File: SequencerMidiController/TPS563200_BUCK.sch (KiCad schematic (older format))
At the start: 13 parts, among them U38 TPS563200

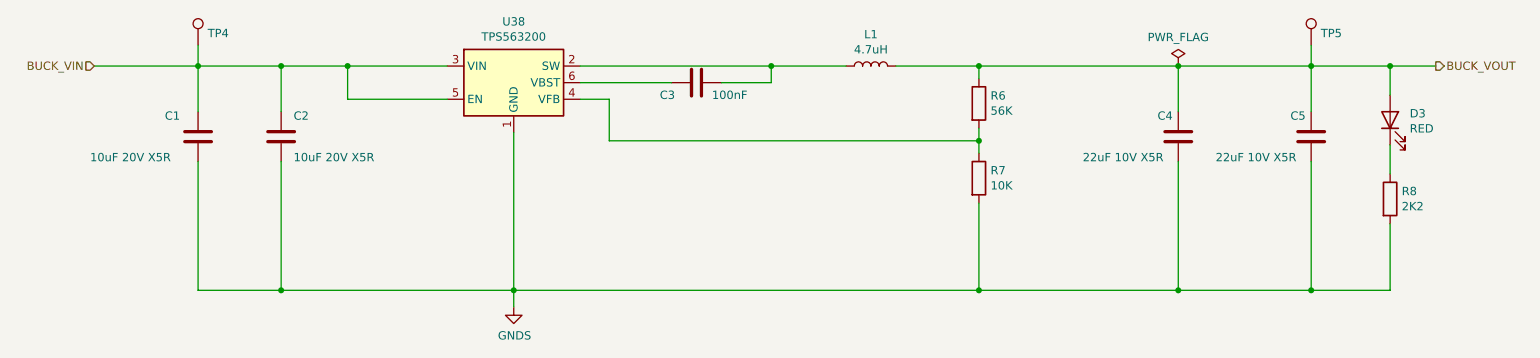
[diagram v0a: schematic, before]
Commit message: RevA Layout draft completed
- Needs tidy up
- Add test points
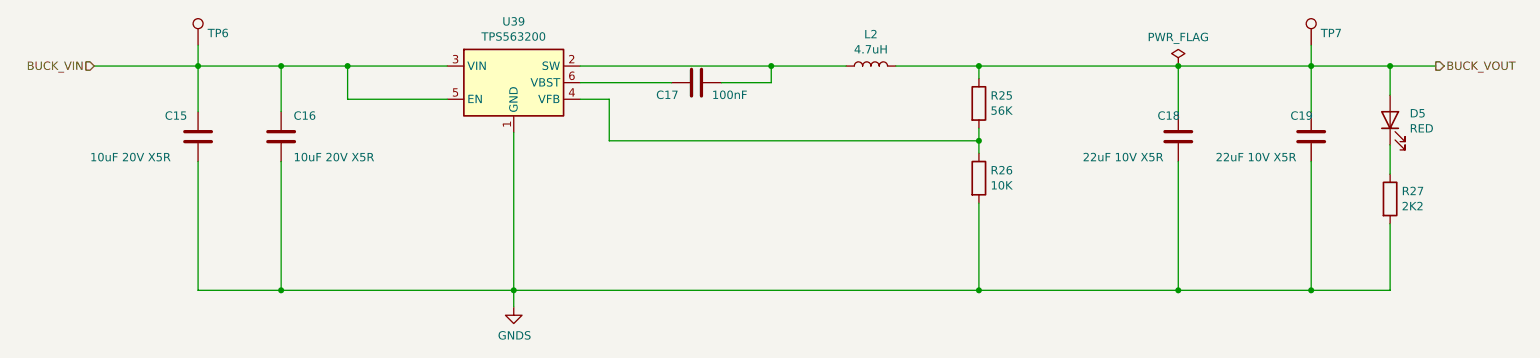
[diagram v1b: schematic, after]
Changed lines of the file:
@@
 AR Path="/60BD3123/60BD5AA5/60BD5C0D" Ref="U38"  Part="1"
 AR Path="/60BD3123/63615DFB/60BD5C0D" Ref="U39"  Part="1"
-F 0 "U38" H 4150 3667 50  0000 C CNN
+F 0 "U39" H 4150 3667 50  0000 C CNN
 F 1 "TPS563200" H 4150 3576 50  0000 C CNN
 F 2 "Package_TO_SOT_SMD:SOT-23-6" H 4200 3050 50  0001 L CNN
 F 3 "http://www.ti.com/lit/ds/symlink/tps563200.pdf" H 4175 3750 50  0001 C CNN
+F 4 "~" H 4150 3300 50  0001 C CNN "LcscNo"
+F 5 "~" H 4150 3300 50  0001 C CNN "Type"
 	1    4150 3300
 	1    0    0    -1
@@
 AR Path="/60BD3123/60BD5AA5/60BD6656" Ref="#PWR0108"  Part="1"
 AR Path="/60BD3123/63615DFB/60BD6656" Ref="#PWR023"  Part="1"
-F 0 "#PWR0108" H 4150 4400 50  0001 C CNN
+F 0 "#PWR023" H 4150 4400 50  0001 C CNN
 F 1 "GNDS" H 4155 4477 50  0000 C CNN
 F 2 "" H 4150 4650 50  0001 C CNN
@@
 AR Path="/60BD3123/60BD5AA5/60BD6867" Ref="C1"  Part="1"
 AR Path="/60BD3123/63615DFB/60BD6867" Ref="C15"  Part="1"
-F 0 "C1" H 2050 3750 50  0000 L CNN
+F 0 "C15" H 2050 3750 50  0000 L CNN
 F 1 "10uF 20V X5R" H 1600 3500 50  0000 L CNN
 F 2 "Resistor_SMD:R_1206_3216Metric_Pad1.30x1.75mm_HandSolder" H 2288 3475 50  0001 C CNN
 F 3 "~" H 2250 3625 50  0001 C CNN
+F 4 "~" H 2250 3625 50  0001 C CNN "LcscNo"
+F 5 "~" H 2250 3625 50  0001 C CNN "Type"
 	1    2250 3625
 	1    0    0    -1
@@
 AR Path="/60BD3123/60BD5AA5/60BD7269" Ref="C2"  Part="1"
 AR Path="/60BD3123/63615DFB/60BD7269" Ref="C16"  Part="1"
-F 0 "C2" H 2825 3750 50  0000 L CNN
+F 0 "C16" H 2825 3750 50  0000 L CNN
 F 1 "10uF 20V X5R" H 2825 3500 50  0000 L CNN
 F 2 "Resistor_SMD:R_1206_3216Metric_Pad1.30x1.75mm_HandSolder" H 2788 3475 50  0001 C CNN
 F 3 "~" H 2750 3625 50  0001 C CNN
+F 4 "~" H 2750 3625 50  0001 C CNN "LcscNo"
+F 5 "~" H 2750 3625 50  0001 C CNN "Type"
 	1    2750 3625
 	1    0    0    -1
@@
 AR Path="/60BD3123/60BD5AA5/60BD7D8E" Ref="L1"  Part="1"
 AR Path="/60BD3123/63615DFB/60BD7D8E" Ref="L2"  Part="1"
-F 0 "L1" V 6490 3200 50  0000 C CNN
+F 0 "L2" V 6490 3200 50  0000 C CNN
 F 1 "4.7uH" V 6399 3200 50  0000 C CNN
 F 2 "Inductor_SMD:L_Taiyo-Yuden_NR-80xx_HandSoldering" H 6300 3200 50  0001 C CNN
 F 3 "https://datasheet.lcsc.com/lcsc/1808311234_SXN-Shun-Xiang-Nuo-Elec-SMNR6028-4R7MT_C266428.pdf" H 6300 3200 50  0001 C CNN
 F 4 "C266428" H 6300 3200 50  0001 C CNN "LcscNo"
+F 5 "~" H 6300 3200 50  0001 C CNN "Type"
 	1    6300 3200
 	0    -1   -1   0
@@
 AR Path="/60BD3123/60BD5AA5/60C2B2AA" Ref="C3"  Part="1"
 AR Path="/60BD3123/63615DFB/60C2B2AA" Ref="C17"  Part="1"
-F 0 "C3" V 5175 3475 50  0000 C CNN
+F 0 "C17" V 5175 3475 50  0000 C CNN
 F 1 "100nF" V 5175 3100 50  0000 C CNN
 F 2 "Capacitor_SMD:C_0805_2012Metric_Pad1.18x1.45mm_HandSolder" H 5288 3150 50  0001 C CNN
 F 3 "~" H 5250 3300 50  0001 C CNN
+F 4 "~" H 5250 3300 50  0001 C CNN "LcscNo"
+F 5 "~" H 5250 3300 50  0001 C CNN "Type"
 	1    5250 3300
 	0    -1   -1   0
@@
 AR Path="/60BD3123/60BD5AA5/60C2D3AE" Ref="R6"  Part="1"
 AR Path="/60BD3123/63615DFB/60C2D3AE" Ref="R25"  Part="1"
-F 0 "R6" H 7020 3471 50  0000 L CNN
+F 0 "R25" H 7020 3471 50  0000 L CNN
 F 1 "56K" H 7020 3380 50  0000 L CNN
 F 2 "Resistor_SMD:R_0805_2012Metric_Pad1.20x1.40mm_HandSolder" V 6880 3425 50  0001 C CNN
 F 3 "~" H 6950 3425 50  0001 C CNN
+F 4 "~" H 6950 3425 50  0001 C CNN "LcscNo"
+F 5 "~" H 6950 3425 50  0001 C CNN "Type"
 	1    6950 3425
 	1    0    0    -1
@@
 AR Path="/60BD3123/60BD5AA5/60C2DA69" Ref="R7"  Part="1"
 AR Path="/60BD3123/63615DFB/60C2DA69" Ref="R26"  Part="1"
-F 0 "R7" H 7020 3921 50  0000 L CNN
+F 0 "R26" H 7020 3921 50  0000 L CNN
 F 1 "10K" H 7020 3830 50  0000 L CNN
 F 2 "Resistor_SMD:R_0805_2012Metric_Pad1.20x1.40mm_HandSolder" V 6880 3875 50  0001 C CNN
 F 3 "~" H 6950 3875 50  0001 C CNN
+F 4 "~" H 6950 3875 50  0001 C CNN "LcscNo"
+F 5 "~" H 6950 3875 50  0001 C CNN "Type"
 	1    6950 3875
 	1    0    0    -1
@@
 AR Path="/60BD3123/60BD5AA5/60C31AEB" Ref="C4"  Part="1"
 AR Path="/60BD3123/63615DFB/60C31AEB" Ref="C18"  Part="1"
-F 0 "C4" H 8025 3750 50  0000 L CNN
+F 0 "C18" H 8025 3750 50  0000 L CNN
 F 1 "22uF 10V X5R" H 7575 3500 50  0000 L CNN
 F 2 "Resistor_SMD:R_1206_3216Metric_Pad1.30x1.75mm_HandSolder" H 8188 3475 50  0001 C CNN
 F 3 "~" H 8150 3625 50  0001 C CNN
+F 4 "~" H 8150 3625 50  0001 C CNN "LcscNo"
+F 5 "~" H 8150 3625 50  0001 C CNN "Type"
 	1    8150 3625
 	1    0    0    -1
@@
 AR Path="/60BD3123/60BD5AA5/60C31AF1" Ref="C5"  Part="1"
 AR Path="/60BD3123/63615DFB/60C31AF1" Ref="C19"  Part="1"
-F 0 "C5" H 8825 3750 50  0000 L CNN
+F 0 "C19" H 8825 3750 50  0000 L CNN
 F 1 "22uF 10V X5R" H 8375 3500 50  0000 L CNN
 F 2 "Resistor_SMD:R_1206_3216Metric_Pad1.30x1.75mm_HandSolder" H 8988 3475 50  0001 C CNN
 F 3 "~" H 8950 3625 50  0001 C CNN
+F 4 "~" H 8950 3625 50  0001 C CNN "LcscNo"
+F 5 "~" H 8950 3625 50  0001 C CNN "Type"
 	1    8950 3625
 	1    0    0    -1
@@
 AR Path="/60BD3123/60BD5AA5/60C3B029" Ref="TP5"  Part="1"
 AR Path="/60BD3123/63615DFB/60C3B029" Ref="TP7"  Part="1"
-F 0 "TP5" H 9008 3147 50  0000 L CNN
+F 0 "TP7" H 9008 3147 50  0000 L CNN
 F 1 "TestPoint" H 9008 3102 50  0001 L CNN
 F 2 "TestPoint:TestPoint_Pad_D1.0mm" H 9150 3075 50  0001 C CNN
 F 3 "~" H 9150 3075 50  0001 C CNN
+F 4 "~" H 8950 3075 50  0001 C CNN "LcscNo"
+F 5 "~" H 8950 3075 50  0001 C CNN "Type"
 	1    8950 3075
 	1    0    0    -1
@@
 AR Path="/60BD3123/60BD5AA5/60C3C725" Ref="TP4"  Part="1"
 AR Path="/60BD3123/63615DFB/60C3C725" Ref="TP6"  Part="1"
-F 0 "TP4" H 2308 3147 50  0000 L CNN
+F 0 "TP6" H 2308 3147 50  0000 L CNN
 F 1 "TestPoint" H 2308 3102 50  0001 L CNN
 F 2 "TestPoint:TestPoint_Pad_D1.0mm" H 2450 3075 50  0001 C CNN
 F 3 "~" H 2450 3075 50  0001 C CNN
+F 4 "~" H 2250 3075 50  0001 C CNN "LcscNo"
+F 5 "~" H 2250 3075 50  0001 C CNN "Type"
 	1    2250 3075
 	1    0    0    -1
@@
 AR Path="/60BD3123/60BD5AA5/60C4D84C" Ref="D3"  Part="1"
 AR Path="/60BD3123/63615DFB/60C4D84C" Ref="D5"  Part="1"
-F 0 "D3" V 9464 3407 50  0000 R CNN
+F 0 "D5" V 9464 3407 50  0000 R CNN
 F 1 "RED" V 9373 3407 50  0000 R CNN
 F 2 "LED_SMD:LED_0805_2012Metric_Pad1.15x1.40mm_HandSolder" H 9425 3525 50  0001 C CNN
 F 3 "~" H 9425 3525 50  0001 C CNN
 F 4 "C2293" H 9425 3525 50  0001 C CNN "LcscNo"
+F 5 "~" H 9425 3525 50  0001 C CNN "Type"
 	1    9425 3525
 	0    -1   -1   0
@@
 AR Path="/60BD3123/60BD5AA5/60C4D852" Ref="R8"  Part="1"
 AR Path="/60BD3123/63615DFB/60C4D852" Ref="R27"  Part="1"
-F 0 "R8" H 9495 4046 50  0000 L CNN
+F 0 "R27" H 9495 4046 50  0000 L CNN
 F 1 "2K2" H 9495 3955 50  0000 L CNN
 F 2 "Resistor_SMD:R_0805_2012Metric_Pad1.20x1.40mm_HandSolder" V 9355 4000 50  0001 C CNN
 F 3 "~" H 9425 4000 50  0001 C CNN
+F 4 "~" H 9425 4000 50  0001 C CNN "LcscNo"
+F 5 "~" H 9425 4000 50  0001 C CNN "Type"
 	1    9425 4000
 	1    0    0    -1
@@
 AR Path="/60BD3123/63615DFB/68A60987" Ref="#FLG0104"  Part="1"
 AR Path="/60BD3123/60BD5AA5/68A60987" Ref="#FLG0103"  Part="1"
-F 0 "#FLG0103" H 8150 3275 50  0001 C CNN
+F 0 "#FLG0104" H 8150 3275 50  0001 C CNN
 F 1 "PWR_FLAG" H 8150 3373 50  0000 C CNN
 F 2 "" H 8150 3200 50  0001 C CNN

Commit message: Completed RevA layout
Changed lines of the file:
@@
 AR Path="/60BD3123/60BD5AA5/60BD5C0D" Ref="U38"  Part="1"
 AR Path="/60BD3123/63615DFB/60BD5C0D" Ref="U39"  Part="1"
-F 0 "U39" H 4150 3667 50  0000 C CNN
+F 0 "U38" H 4150 3667 50  0000 C CNN
 F 1 "TPS563200" H 4150 3576 50  0000 C CNN
 F 2 "Package_TO_SOT_SMD:SOT-23-6" H 4200 3050 50  0001 L CNN
@@
 AR Path="/60BD3123/60BD5AA5/60BD6656" Ref="#PWR0108"  Part="1"
 AR Path="/60BD3123/63615DFB/60BD6656" Ref="#PWR023"  Part="1"
-F 0 "#PWR023" H 4150 4400 50  0001 C CNN
+F 0 "#PWR0108" H 4150 4400 50  0001 C CNN
 F 1 "GNDS" H 4155 4477 50  0000 C CNN
 F 2 "" H 4150 4650 50  0001 C CNN
@@
 AR Path="/60BD3123/60BD5AA5/60BD6867" Ref="C1"  Part="1"
 AR Path="/60BD3123/63615DFB/60BD6867" Ref="C15"  Part="1"
-F 0 "C15" H 2050 3750 50  0000 L CNN
+F 0 "C1" H 2050 3750 50  0000 L CNN
 F 1 "10uF 20V X5R" H 1600 3500 50  0000 L CNN
 F 2 "Resistor_SMD:R_1206_3216Metric_Pad1.30x1.75mm_HandSolder" H 2288 3475 50  0001 C CNN
@@
 AR Path="/60BD3123/60BD5AA5/60BD7269" Ref="C2"  Part="1"
 AR Path="/60BD3123/63615DFB/60BD7269" Ref="C16"  Part="1"
-F 0 "C16" H 2825 3750 50  0000 L CNN
+F 0 "C2" H 2825 3750 50  0000 L CNN
 F 1 "10uF 20V X5R" H 2825 3500 50  0000 L CNN
 F 2 "Resistor_SMD:R_1206_3216Metric_Pad1.30x1.75mm_HandSolder" H 2788 3475 50  0001 C CNN
@@
 AR Path="/60BD3123/60BD5AA5/60BD7D8E" Ref="L1"  Part="1"
 AR Path="/60BD3123/63615DFB/60BD7D8E" Ref="L2"  Part="1"
-F 0 "L2" V 6490 3200 50  0000 C CNN
+F 0 "L1" V 6490 3200 50  0000 C CNN
 F 1 "4.7uH" V 6399 3200 50  0000 C CNN
 F 2 "Inductor_SMD:L_Taiyo-Yuden_NR-80xx_HandSoldering" H 6300 3200 50  0001 C CNN
@@
 AR Path="/60BD3123/60BD5AA5/60C2B2AA" Ref="C3"  Part="1"
 AR Path="/60BD3123/63615DFB/60C2B2AA" Ref="C17"  Part="1"
-F 0 "C17" V 5175 3475 50  0000 C CNN
+F 0 "C3" V 5175 3475 50  0000 C CNN
 F 1 "100nF" V 5175 3100 50  0000 C CNN
 F 2 "Capacitor_SMD:C_0805_2012Metric_Pad1.18x1.45mm_HandSolder" H 5288 3150 50  0001 C CNN
@@
 AR Path="/60BD3123/60BD5AA5/60C2D3AE" Ref="R6"  Part="1"
 AR Path="/60BD3123/63615DFB/60C2D3AE" Ref="R25"  Part="1"
-F 0 "R25" H 7020 3471 50  0000 L CNN
+F 0 "R6" H 7020 3471 50  0000 L CNN
 F 1 "56K" H 7020 3380 50  0000 L CNN
 F 2 "Resistor_SMD:R_0805_2012Metric_Pad1.20x1.40mm_HandSolder" V 6880 3425 50  0001 C CNN
@@
 AR Path="/60BD3123/60BD5AA5/60C2DA69" Ref="R7"  Part="1"
 AR Path="/60BD3123/63615DFB/60C2DA69" Ref="R26"  Part="1"
-F 0 "R26" H 7020 3921 50  0000 L CNN
+F 0 "R7" H 7020 3921 50  0000 L CNN
 F 1 "10K" H 7020 3830 50  0000 L CNN
 F 2 "Resistor_SMD:R_0805_2012Metric_Pad1.20x1.40mm_HandSolder" V 6880 3875 50  0001 C CNN
@@
 AR Path="/60BD3123/60BD5AA5/60C31AEB" Ref="C4"  Part="1"
 AR Path="/60BD3123/63615DFB/60C31AEB" Ref="C18"  Part="1"
-F 0 "C18" H 8025 3750 50  0000 L CNN
+F 0 "C4" H 8025 3750 50  0000 L CNN
 F 1 "22uF 10V X5R" H 7575 3500 50  0000 L CNN
 F 2 "Resistor_SMD:R_1206_3216Metric_Pad1.30x1.75mm_HandSolder" H 8188 3475 50  0001 C CNN
@@
 AR Path="/60BD3123/60BD5AA5/60C31AF1" Ref="C5"  Part="1"
 AR Path="/60BD3123/63615DFB/60C31AF1" Ref="C19"  Part="1"
-F 0 "C19" H 8825 3750 50  0000 L CNN
+F 0 "C5" H 8825 3750 50  0000 L CNN
 F 1 "22uF 10V X5R" H 8375 3500 50  0000 L CNN
 F 2 "Resistor_SMD:R_1206_3216Metric_Pad1.30x1.75mm_HandSolder" H 8988 3475 50  0001 C CNN
@@
 AR Path="/60BD3123/60BD5AA5/60C3B029" Ref="TP5"  Part="1"
 AR Path="/60BD3123/63615DFB/60C3B029" Ref="TP7"  Part="1"
-F 0 "TP7" H 9008 3147 50  0000 L CNN
+F 0 "TP5" H 9008 3147 50  0000 L CNN
 F 1 "TestPoint" H 9008 3102 50  0001 L CNN
 F 2 "TestPoint:TestPoint_Pad_D1.0mm" H 9150 3075 50  0001 C CNN
@@
 AR Path="/60BD3123/60BD5AA5/60C3C725" Ref="TP4"  Part="1"
 AR Path="/60BD3123/63615DFB/60C3C725" Ref="TP6"  Part="1"
-F 0 "TP6" H 2308 3147 50  0000 L CNN
+F 0 "TP4" H 2308 3147 50  0000 L CNN
 F 1 "TestPoint" H 2308 3102 50  0001 L CNN
 F 2 "TestPoint:TestPoint_Pad_D1.0mm" H 2450 3075 50  0001 C CNN
@@
 AR Path="/60BD3123/60BD5AA5/60C4D84C" Ref="D3"  Part="1"
 AR Path="/60BD3123/63615DFB/60C4D84C" Ref="D5"  Part="1"
-F 0 "D5" V 9464 3407 50  0000 R CNN
+F 0 "D3" V 9464 3407 50  0000 R CNN
 F 1 "RED" V 9373 3407 50  0000 R CNN
 F 2 "LED_SMD:LED_0805_2012Metric_Pad1.15x1.40mm_HandSolder" H 9425 3525 50  0001 C CNN
@@
 AR Path="/60BD3123/60BD5AA5/60C4D852" Ref="R8"  Part="1"
 AR Path="/60BD3123/63615DFB/60C4D852" Ref="R27"  Part="1"
-F 0 "R27" H 9495 4046 50  0000 L CNN
+F 0 "R8" H 9495 4046 50  0000 L CNN
 F 1 "2K2" H 9495 3955 50  0000 L CNN
 F 2 "Resistor_SMD:R_0805_2012Metric_Pad1.20x1.40mm_HandSolder" V 9355 4000 50  0001 C CNN
@@
 AR Path="/60BD3123/63615DFB/68A60987" Ref="#FLG0104"  Part="1"
 AR Path="/60BD3123/60BD5AA5/68A60987" Ref="#FLG0103"  Part="1"
-F 0 "#FLG0104" H 8150 3275 50  0001 C CNN
+F 0 "#FLG0103" H 8150 3275 50  0001 C CNN
 F 1 "PWR_FLAG" H 8150 3373 50  0000 C CNN
 F 2 "" H 8150 3200 50  0001 C CNN
